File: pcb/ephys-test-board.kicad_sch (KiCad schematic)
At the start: 9 parts, among them J1 Conn_02x10_Odd_Even, J8 BM03B-SRSS-TB

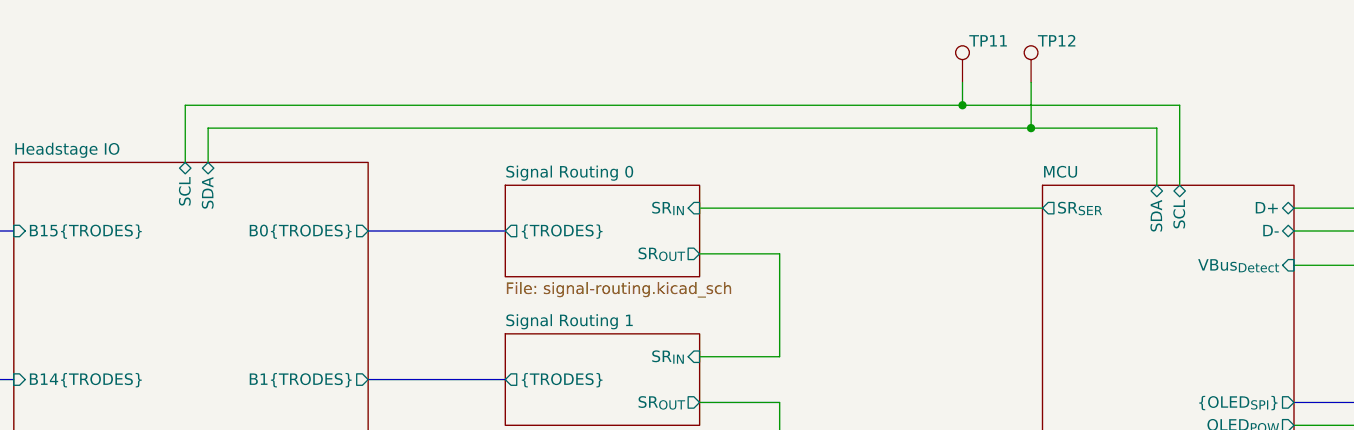
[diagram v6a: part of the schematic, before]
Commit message: Firmware work
- Added mode seleciton capabilites
- Started on channel selection, etc
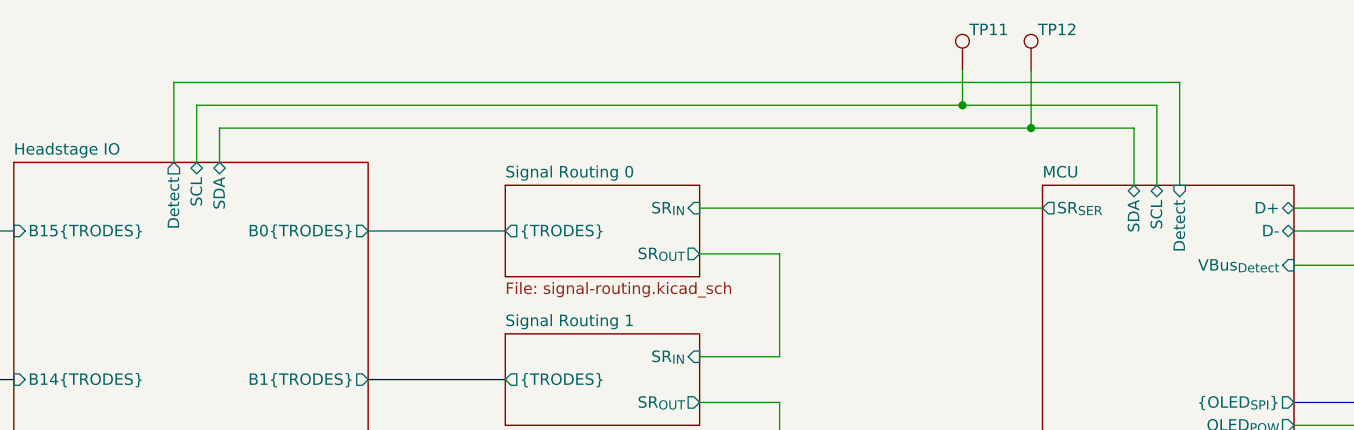
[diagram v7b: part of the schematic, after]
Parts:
- J1: value Conn_02x10_Odd_Even -> 10129383-910002ALF
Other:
- sheet Headstage IO ports: added Detect; removed none
- sheet MCU ports: added Detect; removed none
- moved on the sheet: TP11, TP12
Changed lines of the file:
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@@
 (kicad_sch
-	(version 20241209)
+	(version 20250114)
 	(generator "eeschema")
 	(generator_version "9.0")
@@
 	(title_block
 		(title "Extracellular Electrophysiology Test Board")
-		(rev "B")
+		(rev "C")
 		(company "Open Ephys, Inc")
 		(comment 1 "Jonathan P. Newman")
@@
 	(wire
 		(pts
-			(xy 96.52 29.21) (xy 182.88 29.21)
+			(xy 97.79 29.21) (xy 182.88 29.21)
+		)
+		(stroke
+			(width 0)
+			(type default)
+		)
+	)
+	(wire
+		(pts
+			(xy 207.01 26.67) (xy 207.01 38.1)
 		)
 		(stroke
@@
 	(wire
 		(pts
-			(xy 207.01 38.1) (xy 207.01 29.21)
+			(xy 204.47 38.1) (xy 204.47 29.21)
 		)
 		(stroke
@@
 	(wire
 		(pts
-			(xy 99.06 35.56) (xy 99.06 31.75)
+			(xy 100.33 35.56) (xy 100.33 31.75)
 		)
 		(stroke
@@
 	(wire
 		(pts
-			(xy 96.52 29.21) (xy 96.52 35.56)
+			(xy 97.79 29.21) (xy 97.79 35.56)
+		)
+		(stroke
+			(width 0)
+			(type default)
+		)
+	)
+	(wire
+		(pts
+			(xy 95.25 35.56) (xy 95.25 26.67)
 		)
 		(stroke
@@
 	(wire
 		(pts
+			(xy 95.25 26.67) (xy 207.01 26.67)
+		)
+		(stroke
+			(width 0)
+			(type default)
+		)
+	)
+	(wire
+		(pts
 			(xy 162.56 45.72) (xy 162.56 57.15)
 		)
@@
 	(wire
 		(pts
-			(xy 190.5 31.75) (xy 204.47 31.75)
+			(xy 190.5 31.75) (xy 201.93 31.75)
 		)
 		(stroke
@@
 	(wire
 		(pts
-			(xy 204.47 31.75) (xy 204.47 38.1)
+			(xy 201.93 31.75) (xy 201.93 38.1)
 		)
 		(stroke
@@
 	(wire
 		(pts
-			(xy 190.5 26.67) (xy 190.5 31.75)
+			(xy 190.5 25.4) (xy 190.5 31.75)
 		)
 		(stroke
@@
 	(wire
 		(pts
-			(xy 99.06 31.75) (xy 190.5 31.75)
+			(xy 100.33 31.75) (xy 190.5 31.75)
 		)
 		(stroke
@@
 	(wire
 		(pts
-			(xy 182.88 29.21) (xy 207.01 29.21)
+			(xy 182.88 29.21) (xy 204.47 29.21)
 		)
 		(stroke
@@
 	(wire
 		(pts
-			(xy 182.88 26.67) (xy 182.88 29.21)
+			(xy 182.88 25.4) (xy 182.88 29.21)
 		)
 		(stroke
@@
 			)
 		)
-		(property "Value" "Conn_02x10_Odd_Even"
+		(property "Value" "10129383-910002ALF"
 			(at 254 111.76 0)
 			(effects
@@
 	(symbol
 		(lib_id "Connector:TestPoint")
-		(at 190.5 26.67 0)
+		(at 190.5 25.4 0)
 		(unit 1)
 		(exclude_from_sim no)
@@
 		(dnp no)
 		(property "Reference" "TP12"
-			(at 191.262 22.098 0)
+			(at 191.262 20.828 0)
 			(effects
 				(font
@@
 		)
 		(property "Value" "VCC"
-			(at 191.262 24.638 0)
+			(at 191.262 23.368 0)
 			(effects
 				(font
@@
 		)
 		(property "Footprint" "TestPoint:TestPoint_Pad_D2.0mm"
-			(at 195.58 26.67 0)
+			(at 195.58 25.4 0)
 			(effects
 				(font
@@
 		)
 		(property "Datasheet" "~"
-			(at 195.58 26.67 0)
+			(at 195.58 25.4 0)
 			(effects
 				(font
@@
 		)
 		(property "Description" "test point"
-			(at 190.5 26.67 0)
+			(at 190.5 25.4 0)
 			(effects
 				(font
@@
 		)
 		(property "Voltage" ""
-			(at 190.5 26.67 0)
+			(at 190.5 25.4 0)
 			(effects
 				(font
@@
 		)
 		(property "Datasheet1" ""
-			(at 190.5 26.67 0)
+			(at 190.5 25.4 0)
 			(effects
 				(font
@@
 		)
 		(property "Part No." ""
-			(at 190.5 26.67 0)
+			(at 190.5 25.4 0)
 			(effects
 				(font
@@
 	(symbol
 		(lib_id "Connector:TestPoint")
-		(at 182.88 26.67 0)
+		(at 182.88 25.4 0)
 		(unit 1)
 		(exclude_from_sim no)
@@
 		(dnp no)
 		(property "Reference" "TP11"
-			(at 183.642 22.098 0)
+			(at 183.642 20.828 0)
 			(effects
 				(font
@@
 		)
 		(property "Value" "VCC"
-			(at 183.642 24.638 0)
+			(at 183.642 23.368 0)
 			(effects
 				(font
@@
 		)
 		(property "Footprint" "TestPoint:TestPoint_Pad_D2.0mm"
-			(at 187.96 26.67 0)
+			(at 187.96 25.4 0)
 			(effects
 				(font
@@
 		)
 		(property "Datasheet" "~"
-			(at 187.96 26.67 0)
+			(at 187.96 25.4 0)
 			(effects
 				(font
@@
 		)
 		(property "Description" "test point"
-			(at 182.88 26.67 0)
+			(at 182.88 25.4 0)
 			(effects
 				(font
@@
 		)
 		(property "Voltage" ""
-			(at 182.88 26.67 0)
+			(at 182.88 25.4 0)
 			(effects
 				(font
@@
 		)
 		(property "Datasheet1" ""
-			(at 182.88 26.67 0)
+			(at 182.88 25.4 0)
 			(effects
 				(font
@@
 		)
 		(property "Part No." ""
-			(at 182.88 26.67 0)
+			(at 182.88 25.4 0)
 			(effects
 				(font
@@
 		)
 		(pin "SDA" bidirectional
-			(at 204.47 38.1 90)
+			(at 201.93 38.1 90)
 			(effects
 				(font
@@
 		)
 		(pin "SCL" bidirectional
-			(at 207.01 38.1 90)
+			(at 204.47 38.1 90)
 			(effects
 				(font
@@
 			)
 		)
+		(pin "Detect" input
+			(at 207.01 38.1 90)
+			(effects
+				(font
+					(size 1.27 1.27)
+				)
+				(justify right)
+			)
+		)
 		(instances
 			(project "ephys-test-board"
@@
 		)
 		(pin "SCL" bidirectional
-			(at 96.52 35.56 90)
+			(at 97.79 35.56 90)
 			(effects
 				(font
@@
 		)
 		(pin "SDA" bidirectional
-			(at 99.06 35.56 90)
+			(at 100.33 35.56 90)
+			(effects
+				(font
+					(size 1.27 1.27)
+				)
+				(justify right)
+			)
+		)
+		(pin "Detect" output
+			(at 95.25 35.56 90)
 			(effects
 				(font

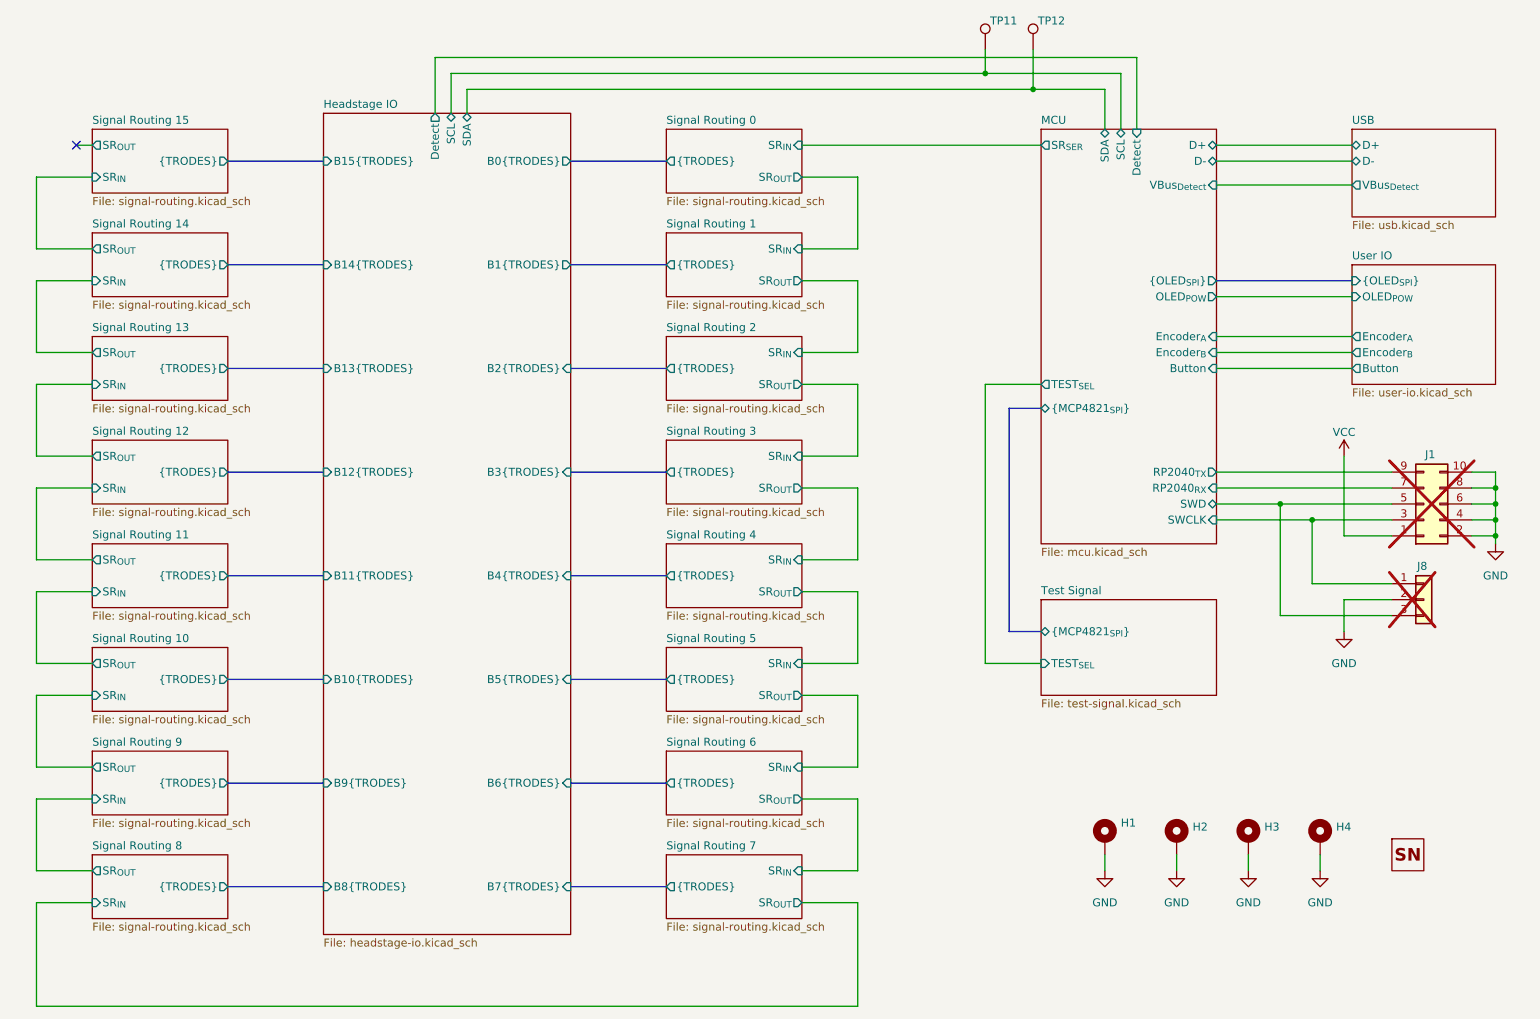
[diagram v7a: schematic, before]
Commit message: Fix electrode coupling
- AC coupling follows attentuation to prevent high-pass filtering
- Remove redundant i2c pullups (can be enabled in MCU if really needed)
- Replace detect line with WP/Detect so that this device can be used to
  program module EEPROM by pulling the line down
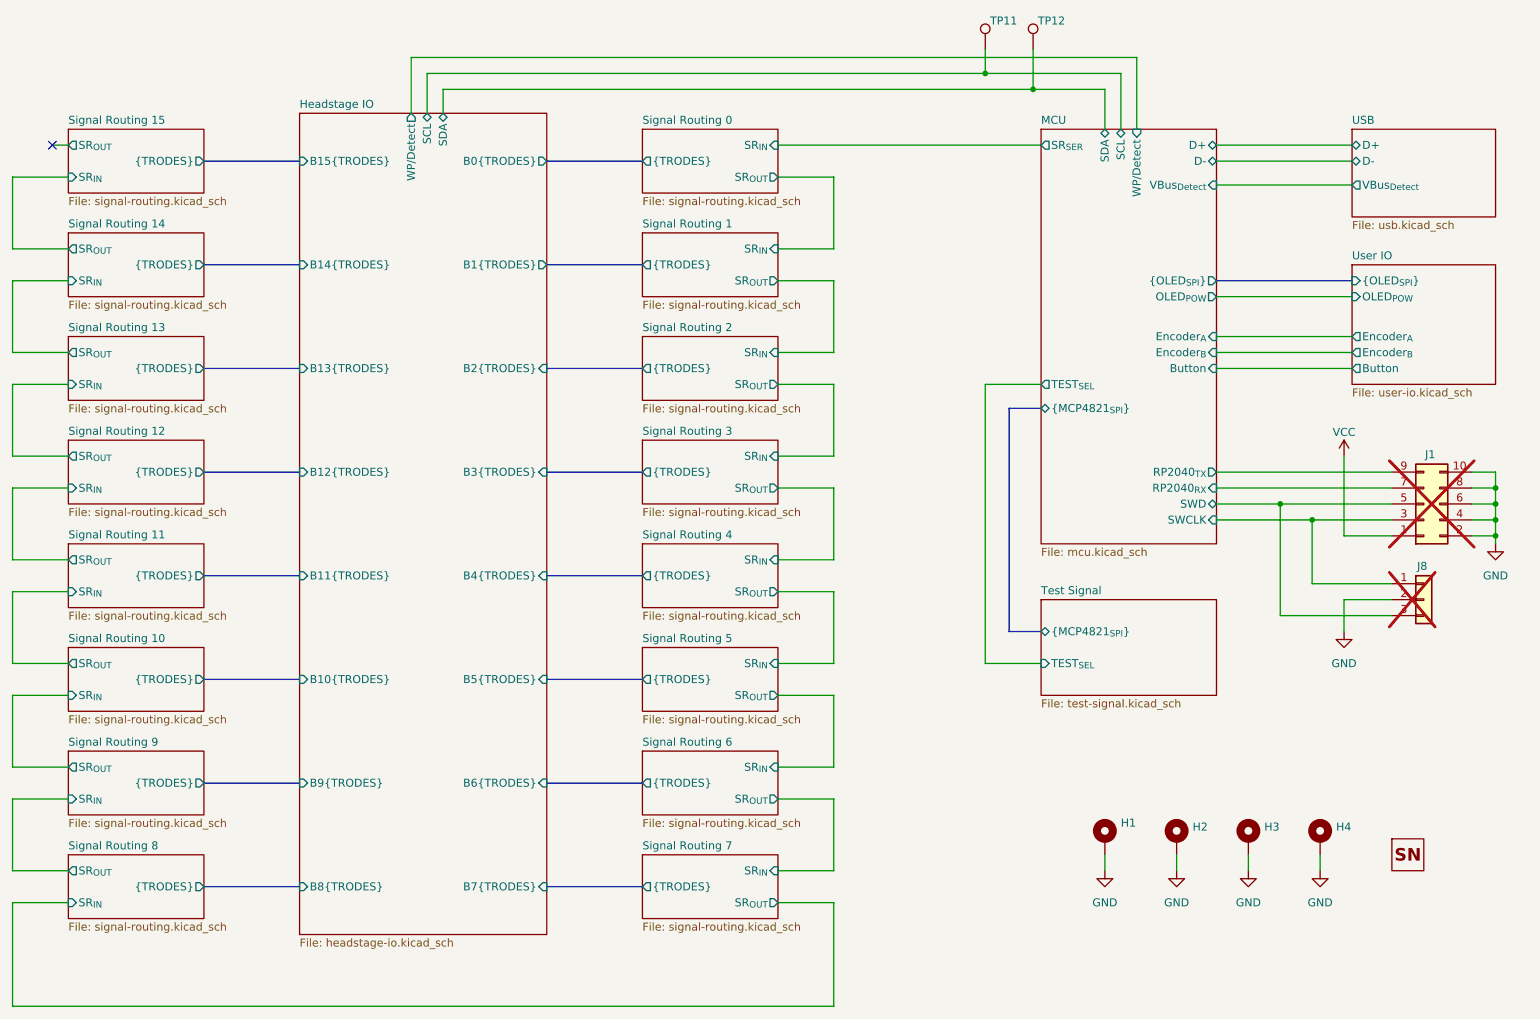
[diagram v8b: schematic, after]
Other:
- sheet Headstage IO ports: added WP/Detect; removed Detect
- sheet MCU ports: added WP/Detect; removed Detect
